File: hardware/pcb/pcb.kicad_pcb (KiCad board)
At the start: 2 copper layers, 41.5 x 66.5 mm, 176 parts, among them J300 Conn_01x02, J301 AudioJack3_Ground_SwitchTR, J400 Conn_02x10_Top_Bottom_Mountin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, J700 USB_B_Micro, U1 AXP209, U100 XC6SLX16-FTG256, U101 W25Q32JVZP, U102 STM32L052K8Ux, U103 PCA9306, U2 SY8008, U200 IS66WVE4M16, U300 WM8960, U400 TC358778, U401 TPS65631W, U402 AP2127K-3.0, U700 USBLC6-2SC6, X100 24.576MHz, Y100 Crystal

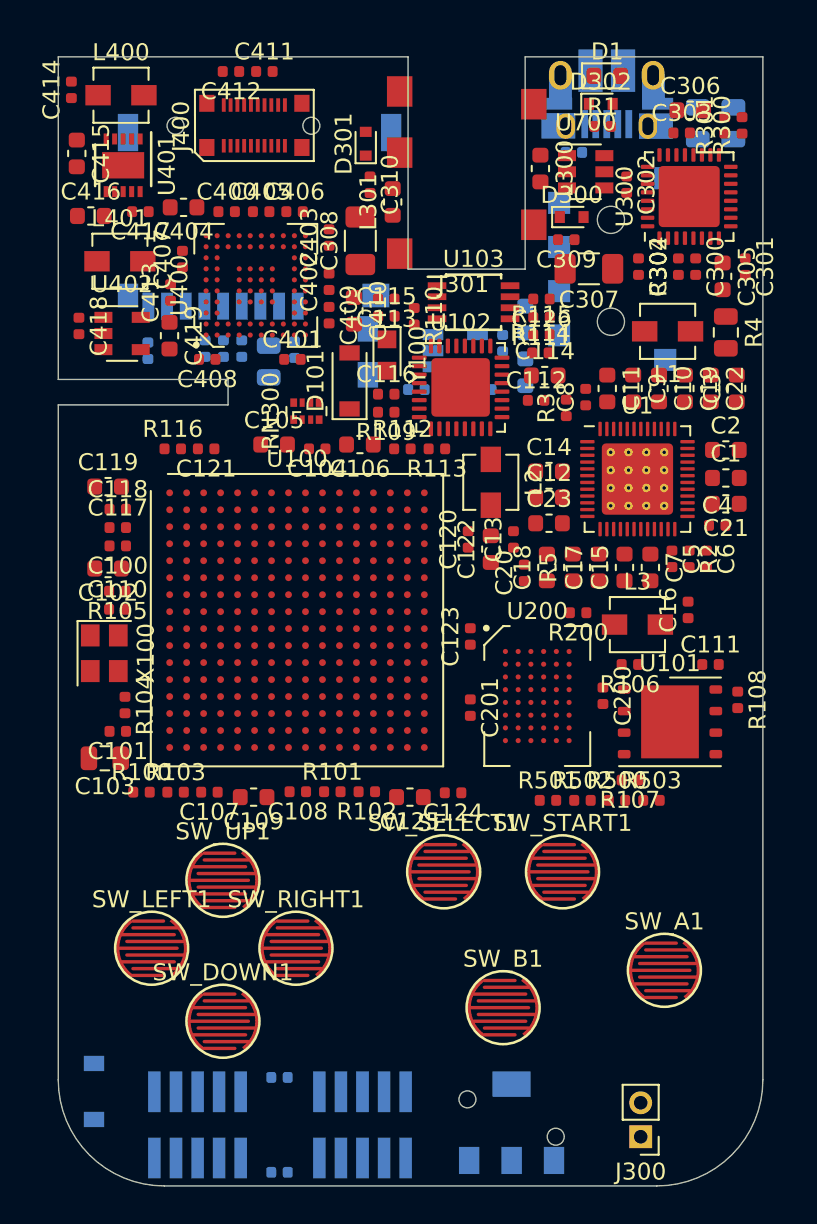
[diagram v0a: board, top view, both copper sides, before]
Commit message: pcb: working on ram/ lcd routing
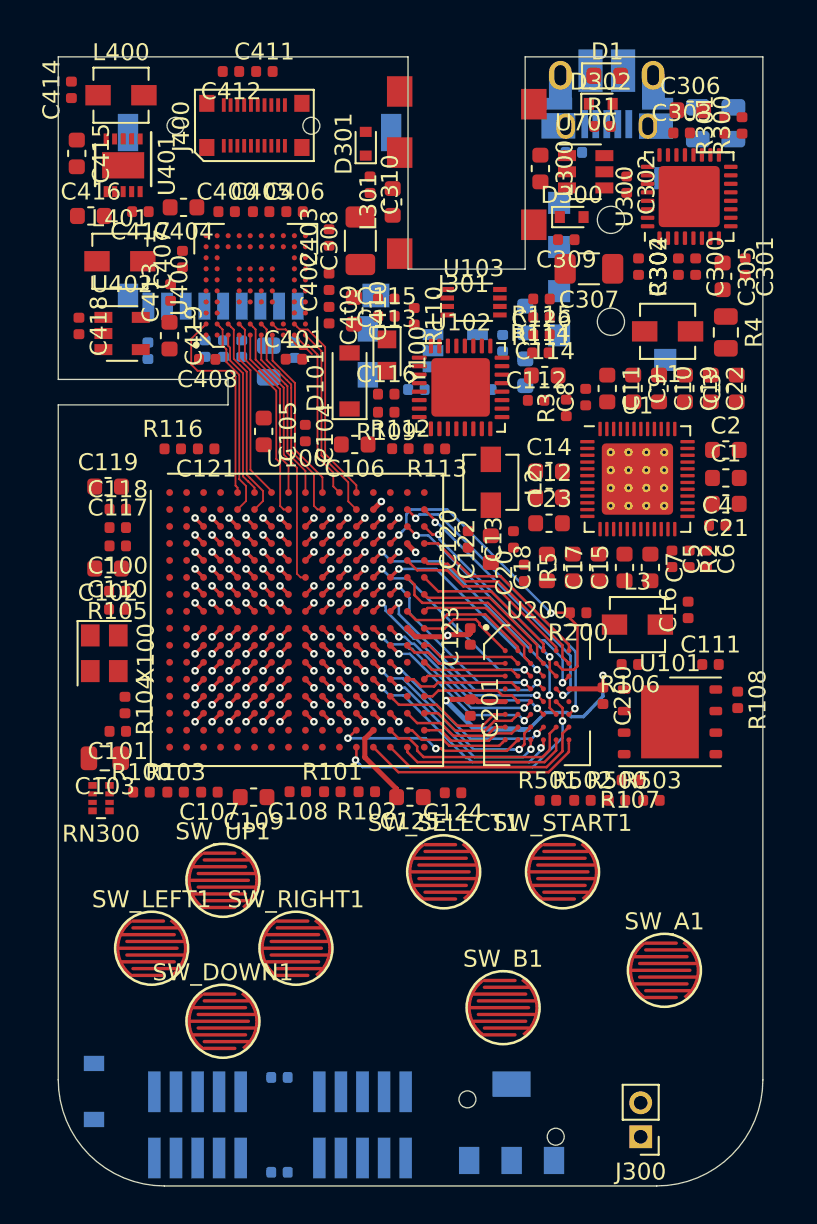
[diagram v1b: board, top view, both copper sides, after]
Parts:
- U103: footprint Package_SO:TSSOP-8_3x3mm_P0.65mm -> Package_SO:VSSOP-8_2.3x2mm_P0.5mm
- moved RN300 25.8 mm to (102.5, 93.7), turned to 180 degrees
- moved C104 1.16 mm to (114.5, 72.2), turned to 270 degrees
- moved C105 0.99 mm to (112.1, 72.1), turned to 270 degrees
- moved C106 0.31 mm to (117.5, 72.8)
- moved R112 0.12 mm to (120.2, 73.1)
- moved C401 0.09 mm to (113.9, 67.8)
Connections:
- ARM_JTAG1 pad 6: Net-(ARM_JTAG1-Pad6) -> (no net)
- ARM_JTAG1 pad 7: Net-(ARM_JTAG1-Pad7) -> (no net)
- ARM_JTAG1 pad 8: Net-(ARM_JTAG1-Pad8) -> (no net)
- ARM_JTAG1 pad 9: Net-(ARM_JTAG1-Pad9) -> (no net)
- FPGA_JTAG1 pad 10: Net-(FPGA_JTAG1-Pad10) -> (no net)
- FPGA_JTAG1 pad 7: Net-(FPGA_JTAG1-Pad7) -> (no net)
- FPGA_JTAG1 pad 9: Net-(FPGA_JTAG1-Pad9) -> (no net)
- J301 pad TN: Net-(J301-PadTN) -> (no net)
- J400 pad 8: Net-(J400-Pad8) -> (no net)
- J700 pad 4: Net-(J700-Pad4) -> (no net)
- R300 pad 2: DAC_SCK -> (no net)
- R301 pad 2: DAC_SDA -> (no net)
- RN300 pad 1: DAC_LRCK -> (no net)
- RN300 pad 2: DAC_BCLK -> (no net)
- RN300 pad 3: DAC_DOUT -> (no net)
- RN300 pad 4: DAC_MCLK -> (no net)
- U1 pad 18: Net-(U1-Pad18) -> (no net)
- U1 pad 2: SYS_SCK -> (no net)
- U1 pad 3: Net-(U1-Pad3) -> (no net)
- U1 pad 30: Net-(U1-Pad30) -> (no net)
- U1 pad 32: Net-(U1-Pad32) -> (no net)
- U1 pad 33: Net-(U1-Pad33) -> (no net)
- U1 pad 5: Net-(U1-Pad5) -> (no net)
- U100 pad A10: Net-(U100-PadA10) -> LCD_D7
- U100 pad A11: BL_EN -> LCD_D4
- U100 pad A12: Net-(U100-PadA12) -> LCD_D2
- U100 pad A13: Net-(U100-PadA13) -> LCD_PCLK
- U100 pad A14: Net-(U100-PadA14) -> LCD_VS
- U100 pad A2: Net-(U100-PadA2) -> (no net)
- U100 pad A3: Net-(U100-PadA3) -> (no net)
- U100 pad A4: Net-(U100-PadA4) -> (no net)
- U100 pad A5: SD_CMD -> LCD_D17
- U100 pad A6: SD_DAT3 -> LCD_D15
- U100 pad A7: Net-(U100-PadA7) -> LCD_D13
- U100 pad A8: DAC_MCLK -> LCD_D11
- U100 pad A9: DAC_LRCK -> LCD_D9
- U100 pad B1: Net-(U100-PadB1) -> (no net)
- U100 pad B10: Net-(U100-PadB10) -> LCD_D8
- U100 pad B12: Net-(U100-PadB12) -> LCD_D5
- U100 pad B14: Net-(U100-PadB14) -> LCD_DE
- U100 pad B2: Net-(U100-PadB2) -> (no net)
- U100 pad B3: Net-(U100-PadB3) -> (no net)
- U100 pad B5: SD_CLK -> LCD_D16
- U100 pad B6: SD_DAT2 -> LCD_D14
- U100 pad B8: DAC_BCLK -> LCD_D12
- U100 pad C1: Net-(U100-PadC1) -> (no net)
- U100 pad C10: Net-(U100-PadC10) -> LCD_D6
- U100 pad C11: Net-(U100-PadC11) -> LCD_D1
- U100 pad C13: Net-(U100-PadC13) -> LCD_D0
- U100 pad C2: Net-(U100-PadC2) -> (no net)
- U100 pad C3: Net-(U100-PadC3) -> (no net)
- U100 pad C5: SD_DAT0 -> SD_D0
- U100 pad C6: Net-(U100-PadC6) -> SD_CMD
- U100 pad C7: LCD_TE -> SD_D2
- U100 pad C8: Net-(U100-PadC8) -> LCD_TE
- U100 pad C9: DAC_DOUT -> (no net)
- U100 pad D1: Net-(U100-PadD1) -> (no net)
- U100 pad D11: Net-(U100-PadD11) -> LCD_HS
- U100 pad D12: Net-(U100-PadD12) -> LCD_CLK
- U100 pad D3: Net-(U100-PadD3) -> (no net)
- U100 pad D5: SD_DAT1 -> SD_D1
- U100 pad D6: Net-(U100-PadD6) -> SD_CLK
- U100 pad D8: Net-(U100-PadD8) -> SD_D3
- U100 pad D9: Net-(U100-PadD9) -> LCD_D3
- U100 pad E1: Net-(U100-PadE1) -> (no net)
- U100 pad E10: Net-(U100-PadE10) -> (no net)
- U100 pad E11: Net-(U100-PadE11) -> (no net)
- U100 pad E12: Net-(U100-PadE12) -> (no net)
- U100 pad E2: Net-(U100-PadE2) -> (no net)
- U100 pad E3: Net-(U100-PadE3) -> (no net)
- U100 pad E4: Net-(U100-PadE4) -> (no net)
- U100 pad E6: Net-(U100-PadE6) -> (no net)
- U100 pad E7: Net-(U100-PadE7) -> (no net)
- U100 pad E8: Net-(U100-PadE8) -> (no net)
- U100 pad F1: Net-(U100-PadF1) -> (no net)
- U100 pad F10: Net-(U100-PadF10) -> (no net)
- U100 pad F12: Net-(U100-PadF12) -> (no net)
- U100 pad F14: /ram/RAM_A7 -> /ram/RAM_A6
- U100 pad F2: Net-(U100-PadF2) -> (no net)
- U100 pad F3: Net-(U100-PadF3) -> (no net)
- U100 pad F4: Net-(U100-PadF4) -> (no net)
- U100 pad F5: Net-(U100-PadF5) -> (no net)
- U100 pad F6: Net-(U100-PadF6) -> (no net)
- U100 pad F7: Net-(U100-PadF7) -> (no net)
- U100 pad F9: Net-(U100-PadF9) -> LCD_D10
- U100 pad G1: Net-(U100-PadG1) -> (no net)
- U100 pad G11: Net-(U100-PadG11) -> (no net)
- U100 pad G12: Net-(U100-PadG12) -> (no net)
- U100 pad G14: /ram/RAM_A6 -> /ram/RAM_A17
- U100 pad G3: Net-(U100-PadG3) -> (no net)
- U100 pad G5: Net-(U100-PadG5) -> (no net)
- U100 pad G6: Net-(U100-PadG6) -> (no net)
- U100 pad H1: Net-(U100-PadH1) -> (no net)
- U100 pad H11: Net-(U100-PadH11) -> (no net)
- U100 pad H14: /ram/RAM_A17 -> /ram/RAM_A7
- U100 pad H2: Net-(U100-PadH2) -> (no net)
- U100 pad H3: Net-(U100-PadH3) -> (no net)
- U100 pad H4: Net-(U100-PadH4) -> (no net)
- U100 pad H5: Net-(U100-PadH5) -> (no net)
- U100 pad J1: Net-(U100-PadJ1) -> (no net)
- U100 pad J11: Net-(U100-PadJ11) -> (no net)
- U100 pad J12: Net-(U100-PadJ12) -> (no net)
- U100 pad J3: Net-(U100-PadJ3) -> (no net)
- U100 pad J4: Net-(U100-PadJ4) -> (no net)
- U100 pad J6: Net-(U100-PadJ6) -> (no net)
- U100 pad K1: Net-(U100-PadK1) -> (no net)
- U100 pad K11: Net-(U100-PadK11) -> (no net)
- U100 pad K12: Net-(U100-PadK12) -> (no net)
- U100 pad K2: Net-(U100-PadK2) -> (no net)
- U100 pad K3: Net-(U100-PadK3) -> (no net)
- U100 pad K5: Net-(U100-PadK5) -> (no net)
- U100 pad K6: Net-(U100-PadK6) -> (no net)
- U100 pad L1: Net-(U100-PadL1) -> (no net)
- U100 pad L10: Net-(U100-PadL10) -> (no net)
- U100 pad L11: Net-(U100-PadL11) -> (no net)
- U100 pad L12: Net-(U100-PadL12) -> (no net)
- U100 pad L3: Net-(U100-PadL3) -> (no net)
- U100 pad L4: Net-(U100-PadL4) -> (no net)
- U100 pad L5: Net-(U100-PadL5) -> (no net)
- U100 pad L7: Net-(U100-PadL7) -> (no net)
- U100 pad L8: Net-(U100-PadL8) -> (no net)
- U100 pad M1: Net-(U100-PadM1) -> (no net)
- U100 pad M10: Net-(U100-PadM10) -> (no net)
- U100 pad M11: Net-(U100-PadM11) -> (no net)
- U100 pad M12: Net-(U100-PadM12) -> (no net)
- U100 pad M13: /ram/RAM_A9 -> /ram/RAM_A10
- U100 pad M14: /ram/RAM_A10 -> /ram/RAM_A9
- U100 pad M2: Net-(U100-PadM2) -> (no net)
- U100 pad M3: Net-(U100-PadM3) -> (no net)
- U100 pad M4: Net-(U100-PadM4) -> (no net)
- U100 pad M5: Net-(U100-PadM5) -> (no net)
- U100 pad M6: Net-(U100-PadM6) -> (no net)
- U100 pad M7: Net-(U100-PadM7) -> (no net)
- U100 pad M9: Net-(U100-PadM9) -> (no net)
- U100 pad N1: Net-(U100-PadN1) -> (no net)
- U100 pad N12: Net-(U100-PadN12) -> (no net)
- U100 pad N3: Net-(U100-PadN3) -> (no net)
- U100 pad N4: Net-(U100-PadN4) -> (no net)
- U100 pad N6: Net-(U100-PadN6) -> (no net)
- U100 pad N9: Net-(U100-PadN9) -> (no net)
- U100 pad P1: Net-(U100-PadP1) -> (no net)
- U100 pad P2: Net-(U100-PadP2) -> (no net)
- U100 pad P4: Net-(U100-PadP4) -> (no net)
- U100 pad P5: Net-(U100-PadP5) -> (no net)
- U100 pad P6: Net-(U100-PadP6) -> (no net)
- U100 pad P7: Net-(U100-PadP7) -> (no net)
- U100 pad R1: Net-(U100-PadR1) -> (no net)
- U100 pad R2: Net-(U100-PadR2) -> (no net)
- U100 pad R5: Net-(U100-PadR5) -> (no net)
- U100 pad R7: Net-(U100-PadR7) -> (no net)
- U100 pad T4: Net-(U100-PadT4) -> (no net)
- U100 pad T5: Net-(U100-PadT5) -> (no net)
- U100 pad T6: Net-(U100-PadT6) -> (no net)
- U100 pad T7: Net-(U100-PadT7) -> (no net)
- U100 pad T8: Net-(U100-PadT8) -> (no net)
- U102 pad 10: Net-(U102-Pad10) -> (no net)
- U102 pad 12: Net-(U102-Pad12) -> (no net)
- U102 pad 14: Net-(U102-Pad14) -> (no net)
- U102 pad 19: Net-(U102-Pad19) -> (no net)
- U102 pad 20: Net-(U102-Pad20) -> (no net)
- U102 pad 25: Net-(U102-Pad25) -> (no net)
- U102 pad 27: BL_PWM -> (no net)
- U300 pad 1: Net-(U300-Pad1) -> (no net)
- U300 pad 15: Net-(U300-Pad15) -> (no net)
- U300 pad 16: Net-(U300-Pad16) -> (no net)
- U300 pad 2: Net-(U300-Pad2) -> (no net)
- U300 pad 23: Net-(U300-Pad23) -> (no net)
- U300 pad 25: Net-(U300-Pad25) -> (no net)
- U300 pad 27: Net-(U300-Pad27) -> (no net)
- U300 pad 3: Net-(U300-Pad3) -> (no net)
- U300 pad 30: Net-(U300-Pad30) -> (no net)
- U300 pad 4: Net-(U300-Pad4) -> (no net)
- U300 pad 5: Net-(U300-Pad5) -> (no net)
- U300 pad 6: Net-(U300-Pad6) -> (no net)
- U400 pad A3: Net-(U400-PadA3) -> (no net)
- U400 pad A4: Net-(U400-PadA4) -> (no net)
- U400 pad A5: Net-(U400-PadA5) -> (no net)
- U400 pad A6: Net-(U400-PadA6) -> (no net)
- U400 pad B3: Net-(U400-PadB3) -> (no net)
- U400 pad B4: Net-(U400-PadB4) -> (no net)
- U400 pad B5: Net-(U400-PadB5) -> (no net)
- U400 pad B6: Net-(U400-PadB6) -> (no net)
- U400 pad B9: MIPI_RESET -> (no net)
- U400 pad C10: Net-(U400-PadC10) -> (no net)
- U400 pad C9: Net-(U400-PadC9) -> (no net)
- U400 pad D10: Net-(U400-PadD10) -> (no net)
- U400 pad D9: Net-(U400-PadD9) -> (no net)
- U400 pad G10: Net-(U400-PadG10) -> (no net)
- U400 pad G9: Net-(U400-PadG9) -> (no net)
- U402 pad 4: Net-(U402-Pad4) -> (no net)
- U700 pad 5: Net-(U700-Pad5) -> (no net)
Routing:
- net (no net): track 0.00 -> 44.5 mm, vias 0 -> 63
- net /ram/RAM_CE_N: track 0.00 -> 19.2 mm, vias 0 -> 2
- net +RAM: track 0.00 -> 18.5 mm, vias 0 -> 2
- net /ram/RAM_DQ6: track 0.00 -> 17.5 mm, vias 0 -> 2
- net LCD_D10: track 0.00 -> 16.4 mm
- net /ram/RAM_DQ5: track 0.00 -> 16.3 mm, vias 0 -> 2
- net /ram/RAM_DQ4: track 0.00 -> 16.1 mm, vias 0 -> 2
- net /ram/RAM_DQ3: track 0.00 -> 15.4 mm, vias 0 -> 2
- net +1V8: track 0.00 -> 13.6 mm, vias 0 -> 7
- net /ram/RAM_DQ2: track 0.00 -> 13.5 mm, vias 0 -> 2
- net /ram/RAM_A20: track 0.00 -> 13.3 mm
- net /ram/RAM_DQ1: track 0.00 -> 12.9 mm, vias 0 -> 2
- net /ram/RAM_A10: track 0.00 -> 12.9 mm, vias 0 -> 2
- net /ram/RAM_A16: track 0.00 -> 12.8 mm, vias 0 -> 2
- net /ram/RAM_DQ7: track 0.00 -> 12.6 mm
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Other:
- copper layers 2 -> 4
- net class Default: clearance 0.15 -> 0.11
- rule trace_clearance: 0.15 -> 0.11
- rule via_min_size: 0.45 -> 0.41

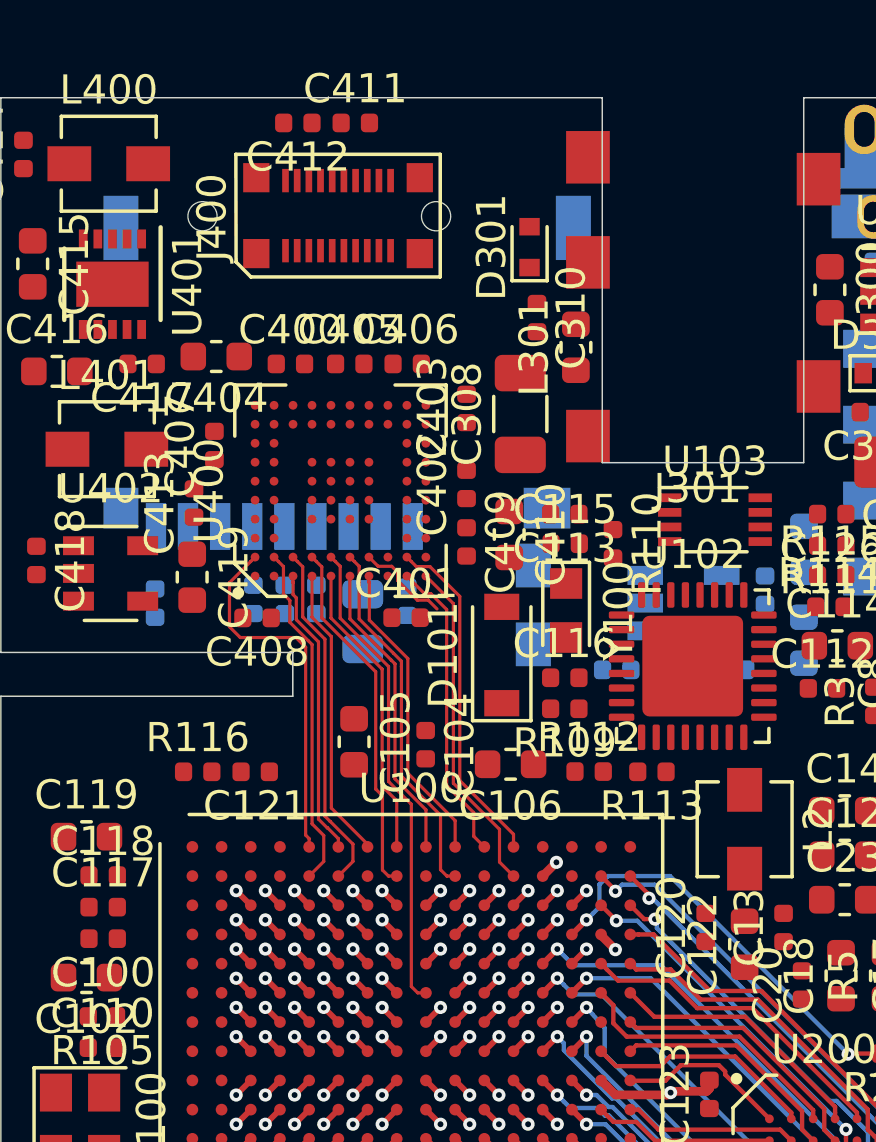
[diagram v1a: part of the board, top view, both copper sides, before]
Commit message: pcb: routing lcd section
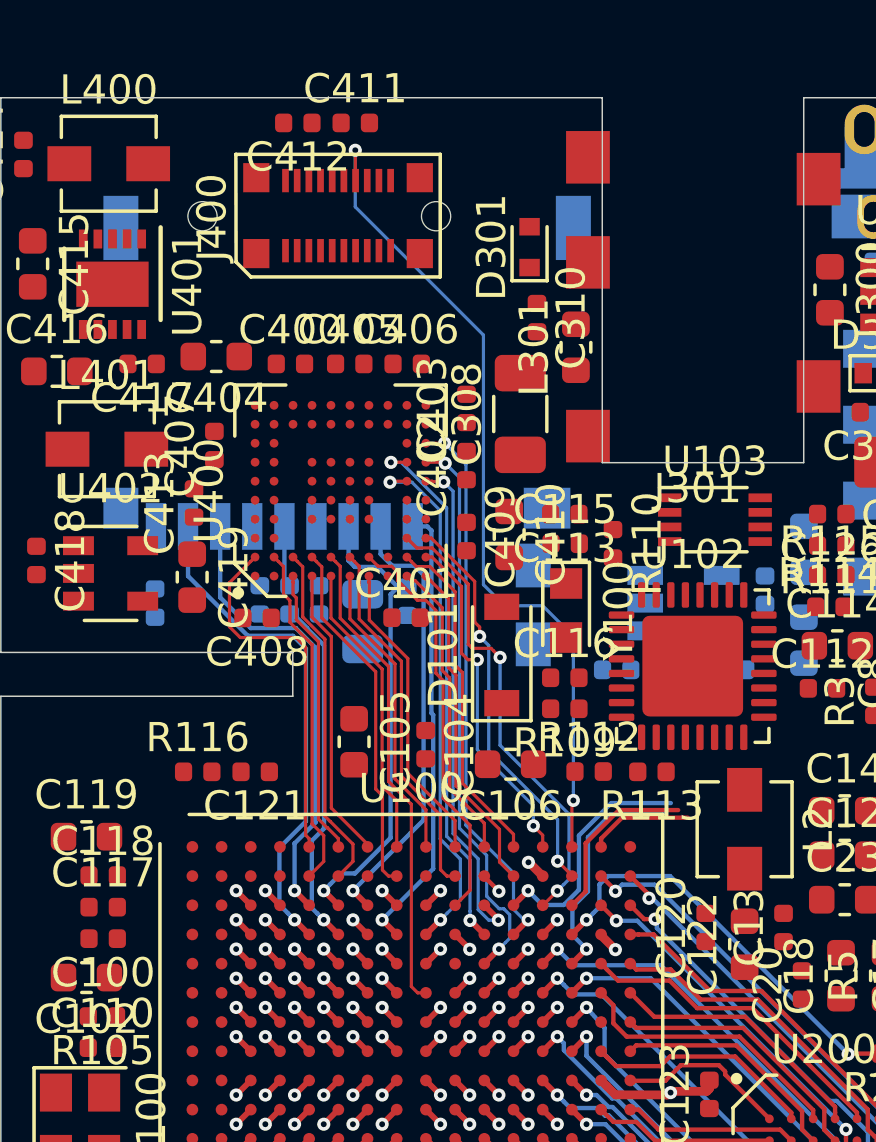
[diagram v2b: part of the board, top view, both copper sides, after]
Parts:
- moved R600 1.24 mm to (109.9, 67.2)
- moved C600 0.86 mm to (108.9, 67.2)
- moved C402 0.65 mm to (116.0, 62.6)
- moved C409 0.18 mm to (116.0, 65.0)
- moved C602 0.09 mm to (110.9, 67.2)
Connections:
- U100 pad A13: LCD_PCLK -> LCD_D3
- U100 pad A14: LCD_VS -> LCD_TE
- U100 pad B14: LCD_DE -> LCD_D1
- U100 pad C11: LCD_D1 -> LCD_CLK
- U100 pad C7: SD_D2 -> SD_D3
- U100 pad C8: LCD_TE -> (no net)
- U100 pad D11: LCD_HS -> LCD_DE
- U100 pad D12: LCD_CLK -> LCD_HS
- U100 pad D8: SD_D3 -> SD_D2
- U100 pad D9: LCD_D3 -> LCD_PCLK
- U100 pad E11: (no net) -> LCD_VS
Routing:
- net LCD_TE: track 0.71 -> 28.8 mm, vias 1 -> 2
- net LCD_VS: track 0.00 -> 19.2 mm, vias 0 -> 2
- net LCD_DE: track 0.00 -> 18.3 mm, vias 0 -> 2
- net LCD_HS: track 0.71 -> 18.9 mm, vias 1 -> 2
- net LCD_PCLK: track 0.00 -> 18.0 mm, vias 0 -> 2
- net SD_D1: track 0.71 -> 17.4 mm
- net LCD_CLK: track 0.71 -> 17.3 mm, vias 1 -> 2
- net SD_CMD: track 0.71 -> 16.0 mm
- net LCD_D0: track 0.71 -> 15.9 mm, vias 1 -> 2
- net SD_D0: track 0.71 -> 15.7 mm
- net SD_D2: track 0.71 -> 15.5 mm
- net SD_D3: track 0.71 -> 15.2 mm
- net LCD_D1: track 0.71 -> 13.8 mm, vias 1 -> 2
- net SD_CLK: track 0.71 -> 12.1 mm
- net LCD_D3: track 0.71 -> 11.9 mm, vias 1 -> 2
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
